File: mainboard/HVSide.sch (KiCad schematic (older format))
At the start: 79 parts, among them J11 CONN_2X2, J17 HV, J18 CONN_1X2, J19 CONN_1X2, J4 CONN_2X2, J8 CONN_1X2, Q1 NTR5105PT1G, Q10 NTR5105PT1G, Q11 NTR5105PT1G, Q12 NTR5105PT1G, Q4 2N7002NXAKR, U15 CD4082, U16 ADCMP350, U19 TCMT1103, U2 TSC211, U24 LM358, U26 TCMT1103, U27 DCDC_ISO_5V, U28 MIC5365-3.3YC5, U29 Si8900, U30 MAX14878AWA+, U7 ADCMP354

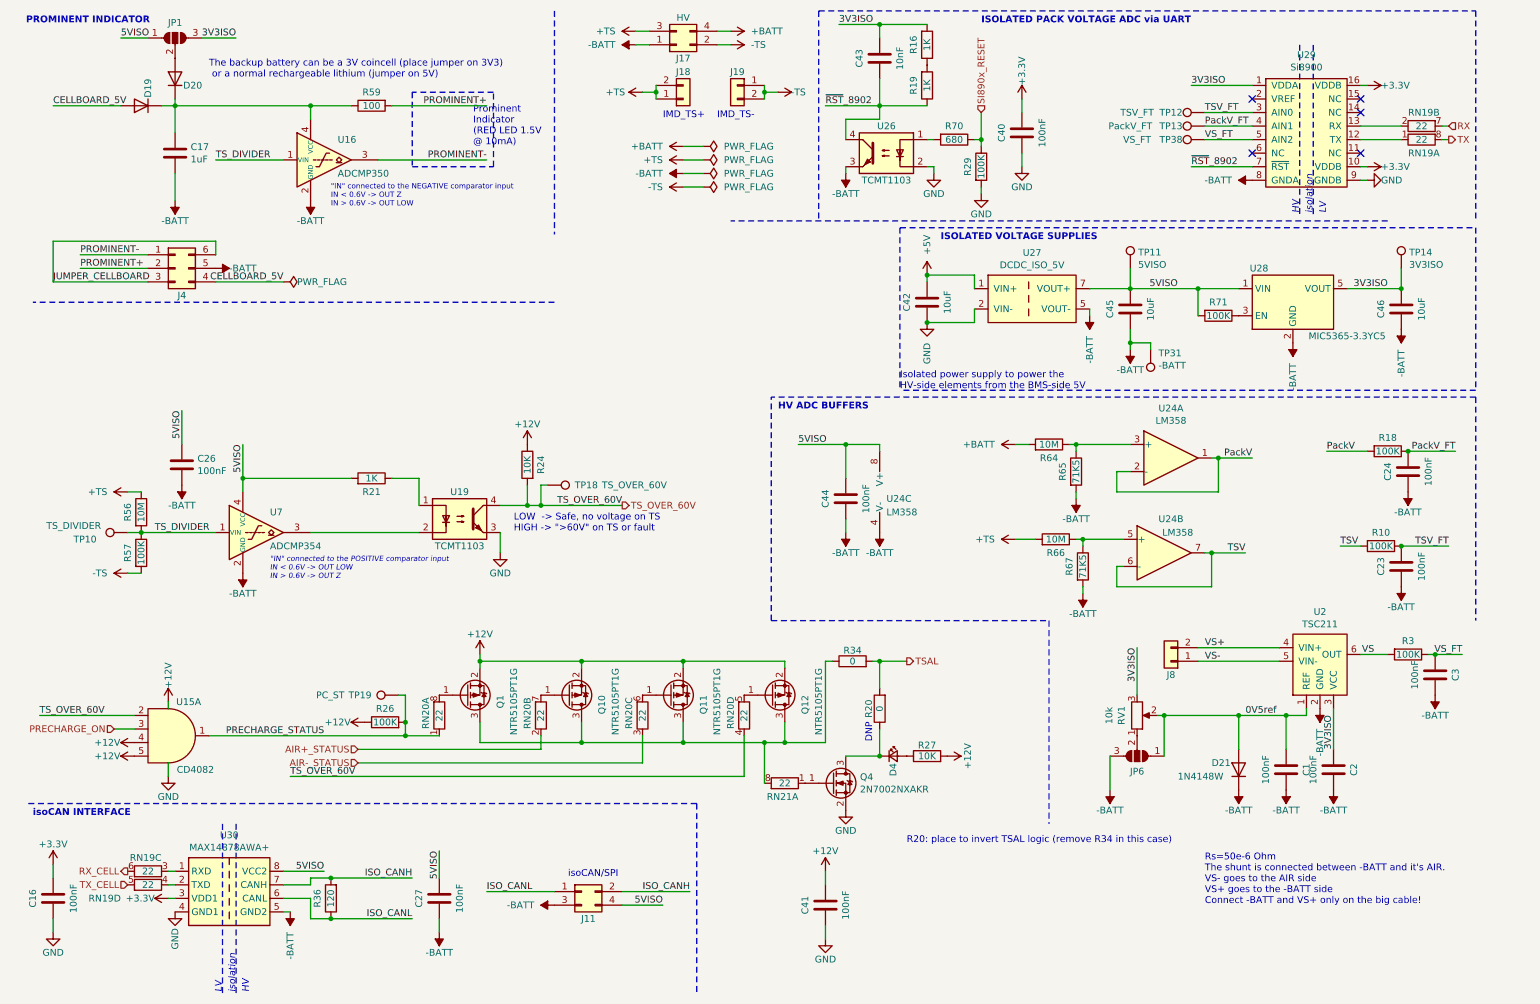
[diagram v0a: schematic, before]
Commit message: Renamed handcart detection
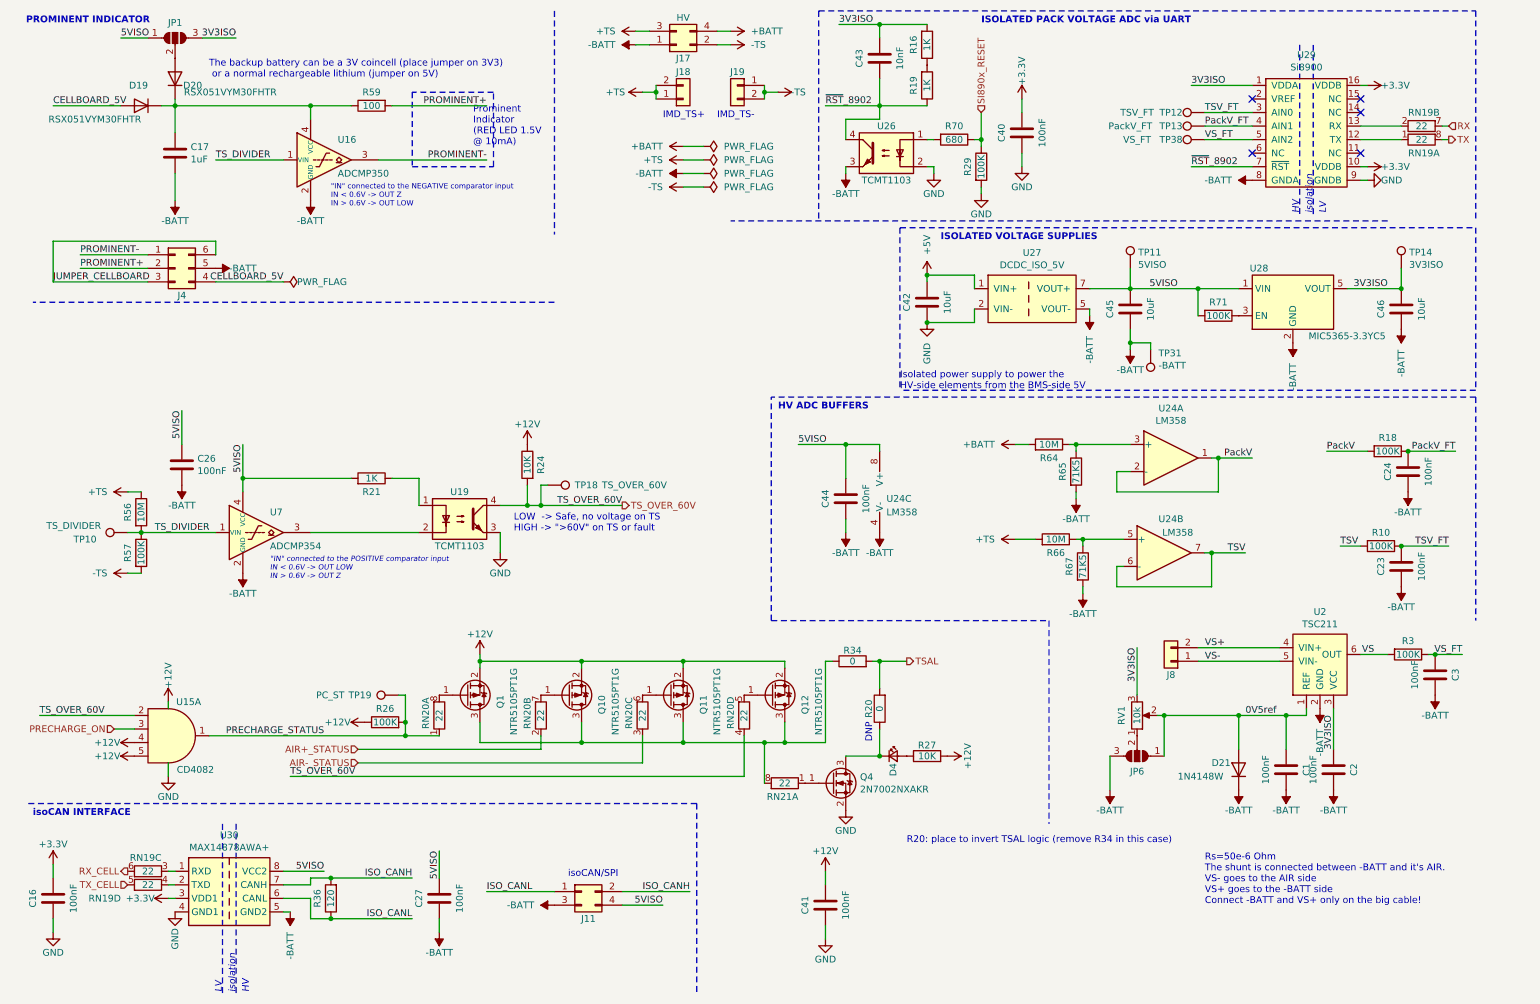
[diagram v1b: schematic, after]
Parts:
- D19, D20: value D -> RSX051VYM30FHTR
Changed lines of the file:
@@
 AR Path="/5B50ED38/60BF5FD9" Ref="D20"  Part="1"
 F 0 "D20" V 1550 800 50  0000 L CNN
-F 1 "D" V 1650 800 50  0001 L CNN
+F 1 "RSX051VYM30FHTR" V 1500 250 50  0000 L CNN
 F 2 "MainBoard:SOD_323HE" H 1600 1000 50  0001 C CNN
 F 3 "~" H 1600 1000 50  0001 C CNN
@@
 AR Path="/60A98674/60C5A929" Ref="D?"  Part="1"
 AR Path="/5B50ED38/60C5A929" Ref="D19"  Part="1"
-F 0 "D19" V 1300 1000 50  0000 L CNN
-F 1 "D" V 1400 1000 50  0001 L CNN
+F 0 "D19" H 1300 1050 50  0000 L CNN
+F 1 "RSX051VYM30FHTR" H 1350 1300 50  0000 L CNN
 F 2 "MainBoard:SOD_323HE" H 1350 1200 50  0001 C CNN
 F 3 "~" H 1350 1200 50  0001 C CNN
@@
 P 8700 5700
 F 0 "RV1" V 8585 5700 50  0000 C CNN
-F 1 "10k" V 8494 5700 50  0000 C CNN
+F 1 "10k" V 8700 5700 50  0000 C CNN
 F 2 "Potentiometer_SMD:Potentiometer_Bourns_3314J_Vertical" H 8700 5700 50  0001 C CNN
 F 3 "~" H 8700 5700 50  0001 C CNN

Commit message: Correction almost finished, Started layouting
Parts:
- removed C41: 100nF, Capacitor_SMD:C_0603_1608Metric, symbol Device:C
- removed C43: 10nF, Capacitor_SMD:C_0603_1608Metric, symbol Device:C
- removed D19, D20: RSX051VYM30FHTR, MainBoard:SOD_323HE, symbol Device:D
- removed J4: CONN_2X2, MainBoard:Molex_Micro-Fit_3.0_43045-0612_2x03_P3.00mm_Vertical, symbol Connector_Generic:Conn_02x03_Counter_Clockwise
- removed JP1: prom_select, Jumper:SolderJumper-3_P1.3mm_Open_RoundedPad1.0x1.5mm, symbol Jumper:SolderJumper_3_Open
- removed Q1, Q10, Q11: NTR5105PT1G, Package_TO_SOT_SMD:SOT-23, symbol Device:Q_PMOS_GSD
- removed R29, R57: 100K, Resistor_SMD:R_0603_1608Metric, symbol Device:R
- removed R34: 0, Resistor_SMD:R_0603_1608Metric, symbol Device:R
- removed R56: 10M, Resistor_SMD:R_2010_5025Metric, symbol Device:R
- removed R59: 100, Resistor_SMD:R_0603_1608Metric, symbol Device:R
- removed R70: 680, Resistor_SMD:R_0603_1608Metric, symbol Device:R
- removed unit 1 of RN19
- removed unit 2 of RN19
- removed TP19: PC_ST, TestPoint:TestPoint_Pad_D1.0mm, symbol Connector:TestPoint
- removed U15: CD4082, Package_SO:TSSOP-14_4.4x5mm_P0.65mm, symbol MainBoard:CD4082
- removed U16: ADCMP350, Package_TO_SOT_SMD:Analog_KS-4, symbol Comparator:ADCMP350
- removed U19, U26: TCMT1103, Package_SO:SOP-4_4.4x2.6mm_P1.27mm, symbol Isolator:TCMT1103
- removed U29: Si8900, Package_SO:SOIC-16W_7.5x10.3mm_P1.27mm, symbol MainBoard:Si8900
- removed U7: ADCMP354, Package_TO_SOT_SMD:Analog_KS-4, symbol Comparator:ADCMP354
- added C4, C5: 100nF, Capacitor_SMD:C_0603_1608Metric, symbol Device:C
- added Q10, Q11, Q17, Q18, Q19, Q20, Q9: 2N7002NXAKR, Package_TO_SOT_SMD:SOT-23, symbol Transistor_FET:2N7002
- added Q21: NTR5105PT1G, Package_TO_SOT_SMD:SOT-23, symbol Device:Q_PMOS_GSD
- added R25: 470, Resistor_SMD:R_0603_1608Metric, symbol Device:R
- added R41, R42: 71K5, Resistor_SMD:R_0603_1608Metric, symbol Device:R
- added RN26: 22, Resistor_SMD:R_Array_Convex_4x0603, symbol Device:R_Pack04_Split
- added RN28: 100K, Resistor_SMD:R_Array_Convex_4x0603, symbol Device:R_Pack04
- added U10, U7: TCMT1103, Package_SO:SOP-4_4.4x2.6mm_P1.27mm, symbol Isolator:TCMT1103
- added U11: ADR280ARTZ, Package_TO_SOT_SMD:SOT-23, symbol Reference_Voltage:MAX6035xxUR25
- added U13: MAX22245, Package_SO:SOIC-8_7.5x5.85mm_P1.27mm, symbol Eagle_Main:MAX22245
- added U15: MAX22246, Package_SO:SOIC-8_7.5x5.85mm_P1.27mm, symbol Eagle_Main:MAX22246
- added U16: ADC124S, Package_SO:VSSOP-10_3x3mm_P0.5mm, symbol Eagle_Main:ADC124S
- added U3: TS3702IPT, Package_SO:TSSOP-8_4.4x3mm_P0.65mm, symbol Eagle_Main:TS3702
- C17: value 1uF -> 100nF; footprint Capacitor_SMD:C_0805_2012Metric -> Capacitor_SMD:C_0603_1608Metric
- D4: value LED_Small -> TS_OFF
- J11: value CONN_2X2 -> isoCAN; footprint MainBoard:Molex_Micro-Fit_3.0_43045-0412_2x02_P3.00mm_Vertical -> Connector_Molex:Molex_Micro-Fit_3.0_43045-0412_2x02_P3.00mm_Vertical; symbol Connector_Generic:Conn_02x02_Odd_Even -> Connector_Generic:Conn_02x02_Top_Bottom
- J17: footprint MainBoard:Molex_Mega-Fit_76829-0104_2x02_P5.70mm_Vertical -> Connector_Molex:Molex_Mega-Fit_76829-0104_2x02_P5.70mm_Vertical; symbol Connector_Generic:Conn_02x02_Odd_Even -> Connector_Generic:Conn_02x02_Top_Bottom
- J18: value CONN_1X2 -> IMD_TS+; footprint MainBoard:Molex_Micro-Fit_3.0_43650-0215_1x02_P3.00mm_Vertical -> Connector_Molex:Molex_Micro-Fit_3.0_43650-0215_1x02_P3.00mm_Vertical
- J19: value CONN_1X2 -> IMD_TS-; footprint MainBoard:Molex_Micro-Fit_3.0_43650-0215_1x02_P3.00mm_Vertical -> Connector_Molex:Molex_Micro-Fit_3.0_43650-0215_1x02_P3.00mm_Vertical
- J8: footprint MainBoard:Molex_Micro-Fit_3.0_43650-0215_1x02_P3.00mm_Vertical -> Connector_Molex:Molex_Micro-Fit_3.0_43650-0215_1x02_P3.00mm_Vertical
- R16: value 1K -> 10M 1%; footprint Resistor_SMD:R_0603_1608Metric -> Resistor_SMD:R_2010_5025Metric
- R19, R21: value 1K -> 270k 10%
- R20: value 0 -> 10M; footprint Resistor_SMD:R_0603_1608Metric -> Resistor_SMD:R_2010_5025Metric
- R24: value 10K -> 470
- R64, R66: value 10M -> 10M 1%
- R65, R67: value 71K5 -> 71K5 1%
- RN19, RN20, RN21: footprint MainBoard:R_network_4x1_bourns_CAY16 -> Resistor_SMD:R_Array_Convex_4x0603
- TP10: value TS_DIVIDER -> CH4
- TP18: value TS_OVER_60V -> CH4_BF
- TP31: footprint MainBoard:TestPoint_GNDedge -> Eagle_Main:TestPoint_GNDedge
- U2: symbol MainBoard:TSC21x -> Eagle_Main:TSC21x
- U27: footprint MainBoard:RFMM -> Eagle_Main:RFMM_0505S; symbol MainBoard:DCDC_ISO_5V -> Eagle_Main:DCDC_ISO_5V
- U30: symbol MainBoard:MAX14878AWA+ -> Eagle_Main:MAX14878AWA+
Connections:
- net +12V: now also Q21.2 (S), RN28.5 (R4.2), U10.4, U7.4; no longer Q12.2 (S), R24.1, R26.1
- net +3V3: now also U13.1 (VDDA), U15.1 (VDDA)
- net +TS: now also R16.1
- net -BATT: now also J17.2 (Pin_2), R19.2, R21.2, C4.2, C5.2, U11.3 (GND), U13.5 (GNDB), U15.5 (GNDB), U16.3 (GND), U3.4 (V-); no longer J17.1 (Pin_1)
- net -TS: now also J17.1 (Pin_1); no longer J17.2 (Pin_2)
- net 3V3ISO: now also C17.1, C4.1, U13.8 (VDDB), U15.8 (VDDB), U16.2 (VA); no longer R16.2
- net 5VISO: now also U10.1, U11.1 (IN), U3.8 (V+), U7.1; no longer R21.2
- net GND: now also Q18.2 (S), RN28.6 (R3.2), RN28.7 (R2.2), RN28.8 (R1.2), U13.4 (GNDA), U15.4 (GNDA)
- net PRECHARGE_STATUS: now also Q19.1 (G), RN28.1 (R1.1), U10.3; no longer R26.2, RN20.1 (R1.1)
- net PackV_FT: now also U16.6 (IN2)
- net TSAL: now also Q12.3 (D), RN26.4 (R4.1), RN28.3 (R3.1); no longer R20.2
- net TSV_FT: now also U16.7 (IN1)
- net VS+: now also J8.1 (Pin_1); no longer J8.2 (Pin_2)
- net VS-: now also J8.2 (Pin_2); no longer J8.1 (Pin_1)
- net VS_FT: now also U16.5 (IN3)
- net PRECHARGE_SENSE: now reaches R21.1
- net PRECHARGE_SENSE: now also R20.1, U3.3 (+)
- net at D4.1 (K), Q4.3 (D): no longer R20.1
- net at RN21.1 (R1.1): no longer Q4.1 (G)
- net at RN21.8 (R1.2): no longer Q12.3 (D)
- net at RN20.8 (R1.2): now also RN20.5 (R4.2), Q19.3 (D), RN28.4 (R4.1)
- net at RN20.7 (R2.2): now also Q9.1 (G)
- net at RN20.6 (R3.2): now also Q10.1 (G)
- net at Q12.1 (G): now also RN20.1 (R1.1); no longer RN20.5 (R4.2)
- net ISO_CANH renamed CAN+
- net CAN+: now also R36.1, U30.6 (CANL)
- removed net ISO_CANL: J11.1 (Pin_1), R36.1, U30.6 (CANL)
- net PackV: no longer names the net of R18.2, U24.1
- net PackV: now also R42.1; no longer U24.2 (-)
- net TSV: no longer names the net of R10.2, U24.7
- net TSV: now also R41.1; no longer U24.6 (-)
- net TS_DIVIDER renamed ADC_CH4
- net ADC_CH4: now also R26.1, C5.1, U16.4 (IN4)
- removed net TS_OVER_60V: R24.2, RN20.4 (R4.1), TP18.1
- net ~RST~_8902 renamed TS_SENSE
- net TS_SENSE: now also R16.2, U3.5 (+)
- new net: R42.2, U24.2 (-)
- new net: R41.2, U24.6 (-)
- new net: Q4.1 (G), RN26.5 (R4.2)
- new net: Q21.1 (G), RN20.4 (R4.1)
- new net: U13.6 (OUT2), U16.8 (MOSI)
- new net: U13.7 (OUT1), U16.1 (~CS~)
- new net: U15.6 (OUT2), U16.10 (SCLK)
- new net: U15.7 (IN1), U16.9 (MISO)
- new net: Q12.2 (S), Q21.3 (D)
- new net: R26.2, TP18.1
- new net: R24.2, U3.7
- new net: R25.2, U3.1
- new net: R25.1, U10.2
- new net: R24.1, U7.2
- new net: Q10.3 (D), Q9.2 (S)
- new net: Q20.2 (S), Q9.3 (D)
- new net: Q10.2 (S), Q11.3 (D)
- new net: Q19.2 (S), Q20.3 (D)
- new net: Q11.1 (G), RN26.8 (R1.2)
- new net: Q11.2 (S), Q17.3 (D)
- new net: Q17.1 (G), RN26.7 (R2.2)
- new net: Q17.2 (S), Q18.3 (D)
- new net: Q18.1 (G), RN26.6 (R3.2)
- new net ADC_MISO: U15.2 (OUT1)
- new net ADC_MOSI: U13.3 (IN2)
- new net ADC_SCLK: U15.3 (IN2)
- new net ADC_~CS~: U13.2 (IN1)
- new net AIR+_OFF: RN26.3 (R3.1)
- new net AIR-_OFF: RN26.2 (R2.1)
- new net CAN-: J11.1 (Pin_1)
- new net PRECHARGE_D: RN26.1 (R1.1)
- new net PRECHARGE_HV_SENSE: R20.2
- new net REF_1.2V: U11.2 (OUT), U3.2 (-), U3.6 (_)
- new net TS_OVER_60V_STATUS: Q20.1 (G), RN28.2 (R2.1), U7.3
- no-connect marks 5 -> 2
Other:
- note added: "For both signals:\nopto ON -> safe (<60V/precharge off)\nopto OFF -> unsafe (>60V/precharge on)"
- note added: "G=0.0071\n600V -> 4.28V\n450V -> 3.19V"
- note added: "G=0.027\n600V -> 16V\n60V -> 1.57V\n45V -> 1.2V\n23V -> 0.6V"
- note added: "ISOLATED PACK VOLTAGE ADC via SPI"
- note added: "LED ON if TS OFF"
- note added: "Rs=50e-6 Ohm\nThe shunt is connected between -BATT and AIR-.\nVS+ goes to the AIR side\nVS- goes to the -BATT side\nConnect -BATT and VS- only on the big cable!"
- note added: "TSAL CONTROL"
- note added: "TSAL:\nL -> TS ON (unsafe)\nH -> TS OFF (safe)"
- note removed: ""IN" connected to the NEGATIVE comparator input\nIN < 0.6V -> OUT Z\nIN > 0.6V -> OUT LOW"
- note removed: ""IN" connected to the POSITIVE comparator input\nIN < 0.6V -> OUT LOW\nIN > 0.6V -> OUT Z"
- note removed: "DNP"
- note removed: "IMD_TS+"
- note removed: "IMD_TS-"
- note removed: "ISOLATED PACK VOLTAGE ADC via UART"
- note removed: "LOW -> Safe, no voltage on TS\nHIGH -> ">60V" on TS or fault"
- note removed: "PROMINENT INDICATOR"
- note removed: "Prominent\nIndicator\n(RED LED 1.5V \n@ 10mA)"
- note removed: "R20: place to invert TSAL logic (remove R34 in this case)"
- note removed: "Rs=50e-6 Ohm\nThe shunt is connected between -BATT and it's AIR.\nVS- goes to the AIR side\nVS+ goes to the -BATT side\nConnect -BATT and VS+ only on the big cable!"
- note removed: "The backup battery can be a 3V coincell (place jumper on 3V3)\n or a normal rechargeable lithium (jumper on 5V)"
- note removed: "isoCAN/SPI"
- moved on the sheet: C23, C24, C26, C27, C40, C42, C44, C45, C46, D4, J11, J17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
